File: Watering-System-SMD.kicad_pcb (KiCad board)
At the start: 2 copper layers, 76 x 30 mm, 23 parts, among them CON1 AVR-ISP-6, J1 Screw_Terminal_1x02, J2 CONN_01X04_MALE, J3 Screw_Terminal_1x04, J4 Screw_Terminal_1x02, M3 MountingHole_3.2mm_M3, Q1 MMBF170, Q2 2N7002, U1 MCP1703, U2 ATTINY84-20SSU, U3 ESP-01

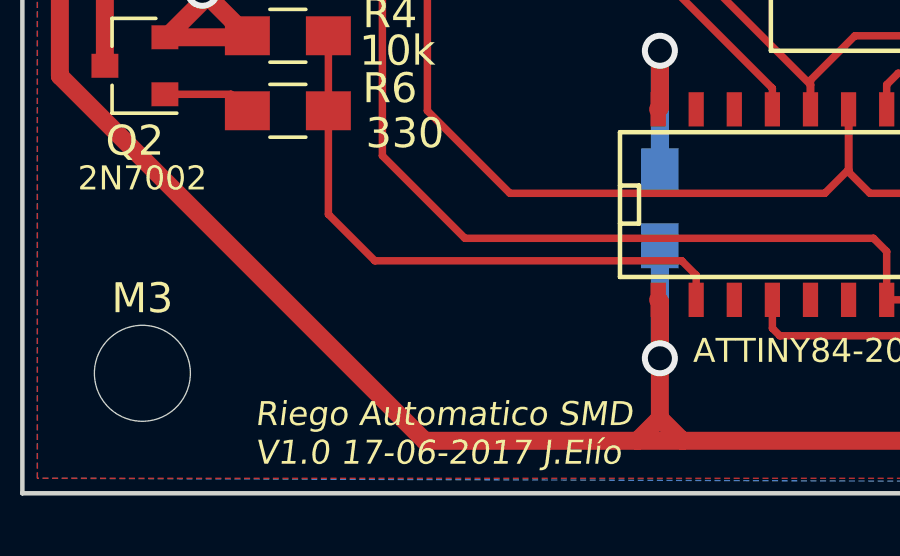
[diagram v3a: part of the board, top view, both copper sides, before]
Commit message: logo added to silkscreen
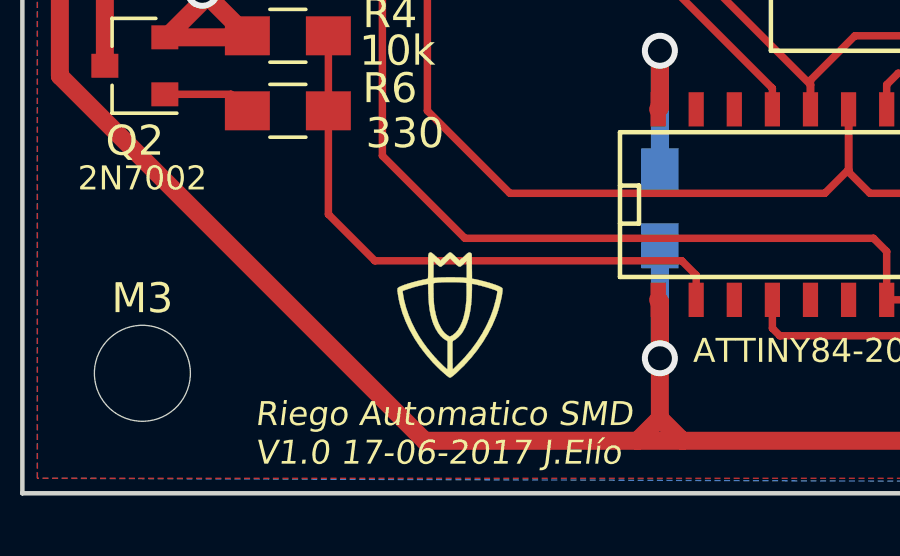
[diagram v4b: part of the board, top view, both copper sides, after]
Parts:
- added G***: LOGO, MisModulos:Logo_peque, F.Cu at (67.2, 93.0)
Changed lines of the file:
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@@
 (kicad_pcb (version 4) (host pcbnew 4.0.6-e0-6349~53~ubuntu16.04.1)
   (general
-    (links 51)
+    (links 0)
     (no_connects 0)
     (area 36.72143 63.678571 145.202382 108.7)
@@
     (tracks 189)
     (zones 0)
-    (modules 23)
+    (modules 24)
     (nets 16)
   )
   (page A4)
   (layers
-    (0 F.Cu signal hide)
-    (31 B.Cu signal hide)
+    (0 F.Cu signal)
+    (31 B.Cu signal)
     (32 B.Adhes user)
     (33 F.Adhes user)
@@
     (pad 1 np_thru_hole circle (at 0 0) (size 3.2 3.2) (drill 3.2) (layers *.Cu *.Mask))
   )
+  (module MisModulos:Logo_peque (layer F.Cu)
+    (at 67.25 93)
+    (fp_text reference G*** (at 0 0) (layer F.SilkS) hide
+      (effects (font (thickness 0.3)))
+    )
+    (fp_text value LOGO (at 0.75 0) (layer F.SilkS) hide
+      (effects (font (thickness 0.3)))
+    )
+    (fp_poly (pts (xy 0.024394 -2.028316) (xy 0.047347 -2.015693) (xy 0.078215 -1.991773) (xy 0.120002 -1.9542)
+      (xy 0.175716 -1.900618) (xy 0.182925 -1.893547) (xy 0.32385 -1.755093) (xy 0.46891 -1.893547)
+      (xy 0.529907 -1.950761) (xy 0.576572 -1.991282) (xy 0.61218 -2.016724) (xy 0.640002 -2.028704)
+      (xy 0.663313 -2.028836) (xy 0.685385 -2.018737) (xy 0.700268 -2.007736) (xy 0.73025 -1.983471)
+      (xy 0.733924 -1.569702) (xy 0.737598 -1.155934) (xy 0.765674 -1.149967) (xy 0.793257 -1.144433)
+      (xy 0.83529 -1.136348) (xy 0.86995 -1.129836) (xy 0.943803 -1.114457) (xy 1.034114 -1.093123)
+      (xy 1.133227 -1.067868) (xy 1.233485 -1.040723) (xy 1.327236 -1.01372) (xy 1.406823 -0.988891)
+      (xy 1.42875 -0.981495) (xy 1.532 -0.94481) (xy 1.612766 -0.913833) (xy 1.673077 -0.88762)
+      (xy 1.714962 -0.865231) (xy 1.740451 -0.845725) (xy 1.749986 -0.832515) (xy 1.756013 -0.79916)
+      (xy 1.754652 -0.745027) (xy 1.746631 -0.673405) (xy 1.732677 -0.587582) (xy 1.71352 -0.490848)
+      (xy 1.689887 -0.386494) (xy 1.662507 -0.277807) (xy 1.632108 -0.168078) (xy 1.599417 -0.060596)
+      (xy 1.565163 0.041349) (xy 1.543532 0.100144) (xy 1.421192 0.38693) (xy 1.275056 0.670748)
+      (xy 1.106721 0.949317) (xy 0.917781 1.22036) (xy 0.709832 1.481595) (xy 0.484468 1.730744)
+      (xy 0.243286 1.965528) (xy 0.2286 1.978879) (xy 0.158745 2.04104) (xy 0.104088 2.086921)
+      (xy 0.062049 2.118388) (xy 0.030049 2.137305) (xy 0.005509 2.145534) (xy -0.003004 2.146252)
+      (xy -0.022227 2.138463) (xy -0.054618 2.11763) (xy -0.094393 2.087623) (xy -0.110954 2.074019)
+      (xy -0.265173 1.938926) (xy -0.41497 1.797518) (xy -0.552128 1.657624) (xy -0.581835 1.6256)
+      (xy -0.807358 1.364111) (xy -1.010046 1.096768) (xy -1.189504 0.824298) (xy -1.34534 0.547427)
+      (xy -1.477158 0.266883) (xy -1.584565 -0.016609) (xy -1.667167 -0.302321) (xy -1.695627 -0.428911)
+      (xy -1.71312 -0.519746) (xy -1.727649 -0.606209) (xy -1.7387 -0.684224) (xy -1.745125 -0.743843)
+      (xy -1.576433 -0.743843) (xy -1.568243 -0.679897) (xy -1.526813 -0.441376) (xy -1.463115 -0.195826)
+      (xy -1.378139 0.053577) (xy -1.272876 0.303657) (xy -1.239281 0.37465) (xy -1.134636 0.578578)
+      (xy -1.023614 0.77066) (xy -0.902792 0.955937) (xy -0.768744 1.139451) (xy -0.618046 1.326242)
+      (xy -0.500976 1.461465) (xy -0.456438 1.510296) (xy -0.404619 1.564955) (xy -0.348503 1.622527)
+      (xy -0.291072 1.6801) (xy -0.235309 1.73476) (xy -0.184198 1.783595) (xy -0.140721 1.82369)
+      (xy -0.107861 1.852133) (xy -0.088601 1.86601) (xy -0.085836 1.8669) (xy -0.083653 1.854666)
+      (xy -0.081644 1.819828) (xy -0.079865 1.765184) (xy -0.078374 1.693528) (xy -0.077228 1.607657)
+      (xy -0.076485 1.510367) (xy -0.076202 1.404454) (xy -0.0762 1.397326) (xy -0.0762 0.929524)
+      (xy 0.0889 0.929524) (xy 0.0889 1.398212) (xy 0.089116 1.504485) (xy 0.089733 1.602315)
+      (xy 0.090701 1.688903) (xy 0.091969 1.761449) (xy 0.09349 1.817157) (xy 0.095212 1.853225)
+      (xy 0.097086 1.866856) (xy 0.0972 1.8669) (xy 0.108613 1.858439) (xy 0.134794 1.835062)
+      (xy 0.172513 1.799772) (xy 0.21854 1.755573) (xy 0.250838 1.724025) (xy 0.49079 1.473105)
+      (xy 0.709066 1.213684) (xy 0.905177 0.94663) (xy 1.078634 0.67281) (xy 1.228947 0.393093)
+      (xy 1.355627 0.108346) (xy 1.458185 -0.180562) (xy 1.536132 -0.472763) (xy 1.562708 -0.60325)
+      (xy 1.57303 -0.661108) (xy 1.578448 -0.699161) (xy 1.579051 -0.722507) (xy 1.574925 -0.736247)
+      (xy 1.566157 -0.745479) (xy 1.565161 -0.746249) (xy 1.539303 -0.75989) (xy 1.492725 -0.778389)
+      (xy 1.429381 -0.800588) (xy 1.353229 -0.825325) (xy 1.268225 -0.851443) (xy 1.178323 -0.877781)
+      (xy 1.087481 -0.903181) (xy 0.999654 -0.926482) (xy 0.918798 -0.946526) (xy 0.84887 -0.962152)
+      (xy 0.794606 -0.972086) (xy 0.7366 -0.980785) (xy 0.736411 -0.811068) (xy 0.729666 -0.546489)
+      (xy 0.710124 -0.300676) (xy 0.677917 -0.074225) (xy 0.633175 0.132269) (xy 0.57603 0.318208)
+      (xy 0.506613 0.482997) (xy 0.425054 0.626038) (xy 0.418808 0.635348) (xy 0.365823 0.704559)
+      (xy 0.302857 0.772896) (xy 0.236567 0.833868) (xy 0.173611 0.880983) (xy 0.15583 0.891751)
+      (xy 0.0889 0.929524) (xy -0.0762 0.929524) (xy -0.0762 0.927752) (xy -0.117475 0.906878)
+      (xy -0.215957 0.843685) (xy -0.308885 0.757301) (xy -0.394889 0.649587) (xy -0.472597 0.522407)
+      (xy -0.540639 0.377622) (xy -0.575732 0.284583) (xy -0.617099 0.152389) (xy -0.650666 0.016107)
+      (xy -0.677045 -0.128342) (xy -0.696848 -0.285034) (xy -0.710686 -0.458044) (xy -0.71917 -0.651451)
+      (xy -0.719864 -0.676489) (xy -0.727761 -0.978327) (xy -0.773456 -0.970481) (xy -0.981164 -0.927938)
+      (xy -1.197977 -0.870676) (xy -1.414358 -0.801231) (xy -1.426392 -0.796989) (xy -1.576433 -0.743843)
+      (xy -1.745125 -0.743843) (xy -1.745758 -0.749711) (xy -1.74831 -0.798592) (xy -1.745842 -0.826788)
+      (xy -1.745809 -0.826891) (xy -1.730573 -0.846287) (xy -1.700048 -0.869216) (xy -1.677073 -0.88231)
+      (xy -1.613389 -0.910856) (xy -1.529602 -0.942799) (xy -1.430543 -0.97668) (xy -1.356778 -0.999829)
+      (xy -0.54896 -0.999829) (xy -0.542695 -0.65549) (xy -0.540128 -0.537551) (xy -0.536958 -0.440594)
+      (xy -0.532893 -0.360198) (xy -0.527639 -0.291948) (xy -0.520904 -0.231424) (xy -0.512395 -0.17421)
+      (xy -0.509754 -0.15875) (xy -0.470844 0.031619) (xy -0.424419 0.199443) (xy -0.369718 0.346664)
+      (xy -0.305975 0.475224) (xy -0.232429 0.587064) (xy -0.201082 0.626381) (xy -0.166505 0.662229)
+      (xy -0.123676 0.699196) (xy -0.078616 0.732894) (xy -0.037345 0.758937) (xy -0.005883 0.772936)
+      (xy 0.001727 0.774179) (xy 0.022035 0.767706) (xy 0.055979 0.750179) (xy 0.096501 0.725275)
+      (xy 0.099737 0.723126) (xy 0.189588 0.648499) (xy 0.270595 0.551208) (xy 0.342363 0.432543)
+      (xy 0.404498 0.293794) (xy 0.456604 0.136251) (xy 0.498286 -0.038797) (xy 0.529149 -0.230059)
+      (xy 0.548799 -0.436247) (xy 0.55684 -0.65607) (xy 0.556424 -0.76835) (xy 0.55245 -1.00965)
+      (xy 0.4826 -1.018394) (xy 0.406724 -1.025782) (xy 0.315024 -1.031311) (xy 0.211715 -1.035029)
+      (xy 0.101011 -1.036981) (xy -0.012874 -1.037216) (xy -0.125724 -1.035778) (xy -0.233324 -1.032715)
+      (xy -0.33146 -1.028072) (xy -0.415918 -1.021898) (xy -0.482481 -1.014237) (xy -0.518955 -1.007339)
+      (xy -0.54896 -0.999829) (xy -1.356778 -0.999829) (xy -1.321041 -1.011044) (xy -1.205925 -1.044431)
+      (xy -1.090025 -1.075386) (xy -0.97817 -1.10245) (xy -0.8763 -1.123954) (xy -0.824375 -1.134155)
+      (xy -0.780229 -1.143255) (xy -0.751213 -1.149722) (xy -0.746125 -1.151043) (xy -0.739948 -1.154358)
+      (xy -0.735029 -1.162119) (xy -0.731226 -1.176946) (xy -0.728397 -1.201457) (xy -0.7264 -1.238269)
+      (xy -0.725094 -1.29) (xy -0.724337 -1.359269) (xy -0.723986 -1.448695) (xy -0.723901 -1.560894)
+      (xy -0.7239 -1.561244) (xy -0.72384 -1.67334) (xy -0.723607 -1.744305) (xy -0.5461 -1.744305)
+      (xy -0.5461 -1.179775) (xy -0.434975 -1.189963) (xy -0.391557 -1.192745) (xy -0.327586 -1.195237)
+      (xy -0.247909 -1.197331) (xy -0.157372 -1.198918) (xy -0.060821 -1.19989) (xy 0.01905 -1.20015)
+      (xy 0.116006 -1.199797) (xy 0.210073 -1.1988) (xy 0.296599 -1.197261) (xy 0.370938 -1.195276)
+      (xy 0.428439 -1.192945) (xy 0.460375 -1.190787) (xy 0.5588 -1.181424) (xy 0.5588 -1.744305)
+      (xy 0.458658 -1.646853) (xy 0.411747 -1.60187) (xy 0.374692 -1.570906) (xy 0.343295 -1.554518)
+      (xy 0.313363 -1.553262) (xy 0.280699 -1.567695) (xy 0.241108 -1.598374) (xy 0.190394 -1.645854)
+      (xy 0.147274 -1.688161) (xy 0.00635 -1.826921) (xy -0.136368 -1.688161) (xy -0.196024 -1.63127)
+      (xy -0.24116 -1.591042) (xy -0.274409 -1.565403) (xy -0.2984 -1.552281) (xy -0.312451 -1.5494)
+      (xy -0.335082 -1.555417) (xy -0.365661 -1.574943) (xy -0.407224 -1.610195) (xy -0.445959 -1.646853)
+      (xy -0.5461 -1.744305) (xy -0.723607 -1.744305) (xy -0.723545 -1.76286) (xy -0.722846 -1.832628)
+      (xy -0.721573 -1.885466) (xy -0.719556 -1.924197) (xy -0.716624 -1.951647) (xy -0.712609 -1.970637)
+      (xy -0.707339 -1.983992) (xy -0.700646 -1.994535) (xy -0.697579 -1.998538) (xy -0.677377 -2.020074)
+      (xy -0.656572 -2.030719) (xy -0.632221 -2.029167) (xy -0.601381 -2.014108) (xy -0.561109 -1.984237)
+      (xy -0.508463 -1.938245) (xy -0.459472 -1.892749) (xy -0.31158 -1.753497) (xy -0.17044 -1.892749)
+      (xy -0.113058 -1.948441) (xy -0.069913 -1.987843) (xy -0.038005 -2.013318) (xy -0.014333 -2.027229)
+      (xy 0.004103 -2.03194) (xy 0.006349 -2.032) (xy 0.024394 -2.028316)) (layer F.SilkS) (width 0.01))
+  )
   (gr_text "Riego Automatico SMD\nV1.0 17-06-2017 J.Elío\n" (at 60.75 97) (layer F.SilkS)

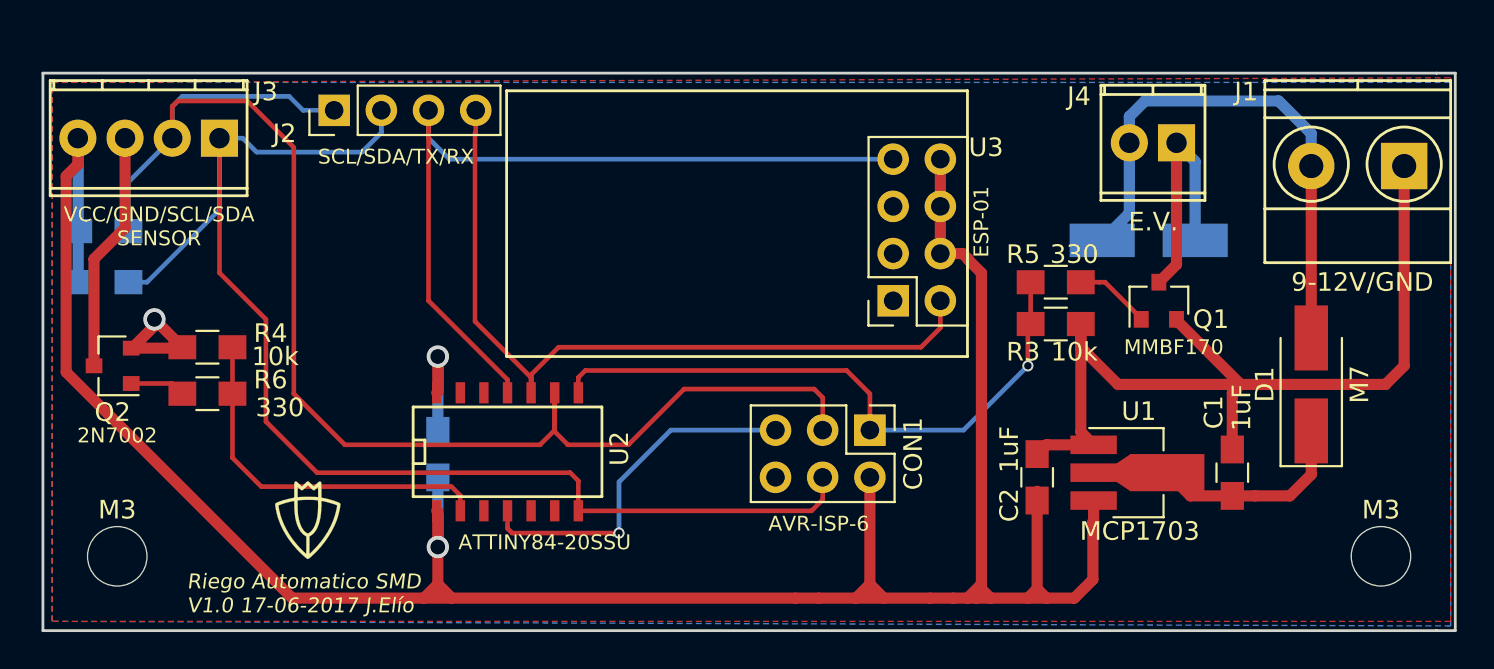
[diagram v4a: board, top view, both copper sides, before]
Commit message: CH-PD routed
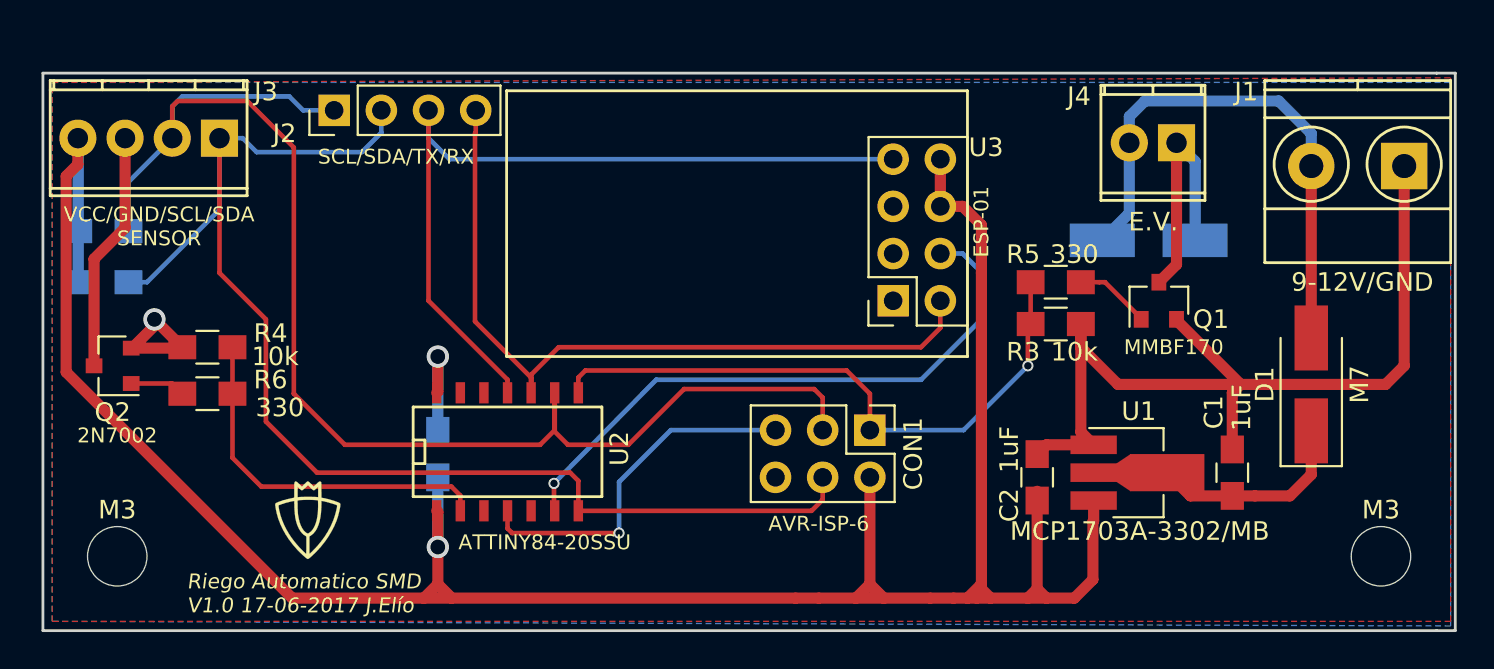
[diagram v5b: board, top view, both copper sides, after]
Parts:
- U1: value MCP1703 -> MCP1703A-3302/MB
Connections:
- U2 pad 6: (no net) -> /CH_PD
- U3 pad 6: VCC -> /CH_PD
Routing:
- net /CH_PD: track 0.00 -> 33.4 mm, vias 0 -> 1
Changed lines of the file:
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@@
 (kicad_pcb (version 4) (host pcbnew 4.0.6-e0-6349~53~ubuntu16.04.1)
   (general
-    (links 0)
+    (links 51)
     (no_connects 0)
     (area 36.72143 63.678571 145.202382 108.7)
     (thickness 1.6)
     (drawings 13)
-    (tracks 189)
+    (tracks 197)
     (zones 0)
     (modules 24)
-    (nets 16)
+    (nets 17)
   )
   (page A4)
@@
   (net 14 "Net-(Q2-Pad1)")
   (net 15 /SENSOR_ON)
+  (net 16 /CH_PD)
   (net_class Default "Esta es la clase de red por defecto."
     (clearance 0.1524)
@@
     (uvia_dia 0.3)
     (uvia_drill 0.1)
+    (add_net /CH_PD)
     (add_net /EV_ON)
     (add_net /RST)
@@
       (net 10 /TX))
     (pad 6 thru_hole oval (at 2.54 2.54 90) (size 1.7 1.7) (drill 1) (layers *.Cu *.Mask)
-      (net 3 VCC))
+      (net 16 /CH_PD))
     (pad 7 thru_hole oval (at 5.08 2.54 90) (size 1.7 1.7) (drill 1) (layers *.Cu *.Mask)
       (net 3 VCC))
@@
       (effects (font (size 1 1) (thickness 0.15)))
     )
-    (fp_text value MCP1703 (at 0.5 3.15) (layer F.SilkS)
+    (fp_text value MCP1703A-3302/MB (at 0.5 3.15) (layer F.SilkS)
       (effects (font (size 1 1) (thickness 0.15)))
     )
@@
       (net 7 /RST))
     (pad 5 smd rect (at 1.27 3.302) (size 0.508 1.143) (layers F.Cu F.Paste F.Mask))
-    (pad 6 smd rect (at 2.54 3.302) (size 0.508 1.143) (layers F.Cu F.Paste F.Mask))
+    (pad 6 smd rect (at 2.54 3.302) (size 0.508 1.143) (layers F.Cu F.Paste F.Mask)
+      (net 16 /CH_PD))
     (pad 7 smd rect (at 3.81 3.302) (size 0.508 1.143) (layers F.Cu F.Paste F.Mask)
       (net 6 /SDA))
@@
   (segment (start 125.25 85.75) (end 126.25 84.75) (width 0.6) (layer F.Cu) (net 2))
   (segment (start 126.25 84.75) (end 126.25 74) (width 0.6) (layer F.Cu) (net 2))
+  (segment (start 101.29 76.17) (end 102.492081 76.17) (width 0.6) (layer F.Cu) (net 3))
+  (segment (start 102.492081 76.17) (end 103.5 77.177919) (width 0.6) (layer F.Cu) (net 3))
+  (segment (start 103.5 77.177919) (end 103.5 79.75) (width 0.6) (layer F.Cu) (net 3))
   (segment (start 106 97.25) (end 104 97.25) (width 0.6) (layer F.Cu) (net 3))
   (segment (start 103.5 96.75) (end 104 97.25) (width 0.6) (layer F.Cu) (net 3))
@@
   (segment (start 103.5 96.5) (end 102.75 97.25) (width 0.6) (layer F.Cu) (net 3))
   (segment (start 103.5 79.75) (end 103.5 96.5) (width 0.6) (layer F.Cu) (net 3))
-  (segment (start 102.782081 79.032081) (end 103.5 79.75) (width 0.6) (layer F.Cu) (net 3))
-  (segment (start 102.782081 79) (end 102.782081 79.032081) (width 0.6) (layer F.Cu) (net 3))
-  (segment (start 101.29 78.71) (end 102.492081 78.71) (width 0.6) (layer F.Cu) (net 3))
-  (segment (start 102.492081 78.71) (end 102.782081 79) (width 0.6) (layer F.Cu) (net 3))
-  (segment (start 101.29 76.17) (end 101.29 78.71) (width 0.6) (layer F.Cu) (net 3))
   (segment (start 101.29 73.63) (end 101.29 76.17) (width 0.6) (layer F.Cu) (net 3))
   (segment (start 103.25 97.25) (end 102.75 97.25) (width 0.6) (layer F.Cu) (net 3))
@@
   (segment (start 75.46 91.7305) (end 74.9795 91.25) (width 0.25) (layer F.Cu) (net 15))
   (segment (start 63.2 83.75) (end 63.2 86.25) (width 0.25) (layer F.Cu) (net 15))
+  (segment (start 80.5 91.0774) (end 80.5 92.512) (width 0.254) (layer F.Cu) (net 16))
+  (segment (start 80.5 92.512) (end 80.54 92.552) (width 0.254) (layer F.Cu) (net 16))
+  (segment (start 86 85.5) (end 80.5 91.0774) (width 0.254) (layer B.Cu) (net 16))
+  (segment (start 80.5 91) (end 80.5 91.0774) (width 0.254) (layer B.Cu) (net 16))
+  (via (at 80.5 91.0774) (size 0.6) (drill 0.4) (layers F.Cu B.Cu) (net 16))
+  (segment (start 100.25 85.5) (end 86 85.5) (width 0.254) (layer B.Cu) (net 16))
+  (segment (start 103.5 82.25) (end 100.25 85.5) (width 0.254) (layer B.Cu) (net 16))
+  (segment (start 103.5 79.717919) (end 103.5 82.25) (width 0.254) (layer B.Cu) (net 16))
+  (segment (start 101.29 78.71) (end 102.492081 78.71) (width 0.254) (layer B.Cu) (net 16))
+  (segment (start 102.492081 78.71) (end 103.5 79.717919) (width 0.254) (layer B.Cu) (net 16))
   (zone (net 2) (net_name GND) (layer B.Cu) (hatch edge 0.508)
     (connect_pads (clearance 0.508))

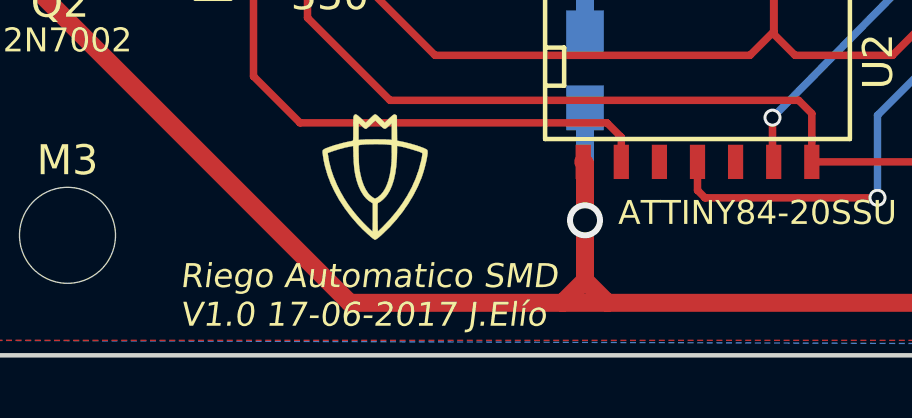
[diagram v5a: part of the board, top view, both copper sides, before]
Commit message: date changed
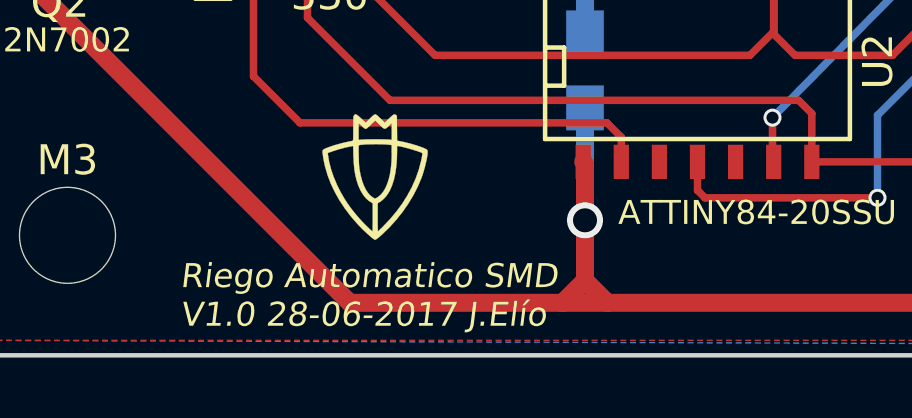
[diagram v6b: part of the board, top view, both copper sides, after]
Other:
- board text added: "Riego Automatico SMD V1.0 28-06-2017 J.Elío"
- board text removed: "Riego Automatico SMD V1.0 17-06-2017 J.Elío"
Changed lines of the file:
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@@
     (links 51)
     (no_connects 0)
-    (area 36.72143 63.678571 145.202382 108.7)
+    (area 52.924999 68.924999 129.075001 99.075001)
     (thickness 1.6)
     (drawings 13)
@@
       (xy 0.004103 -2.03194) (xy 0.006349 -2.032) (xy 0.024394 -2.028316)) (layer F.SilkS) (width 0.01))
   )
-  (gr_text "Riego Automatico SMD\nV1.0 17-06-2017 J.Elío\n" (at 60.75 97) (layer F.SilkS)
+  (gr_text "Riego Automatico SMD\nV1.0 28-06-2017 J.Elío\n" (at 60.75 97) (layer F.SilkS)
     (effects (font (size 0.8 0.8) (thickness 0.15) italic) (justify left))
   )
